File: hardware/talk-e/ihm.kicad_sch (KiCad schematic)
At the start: 17 parts, among them J1 Conn_01x04_Socket, SW1 SW_Push, SW2 SW_Push, SW3 SW_Push, SW4 SS-12D00-G 4 E, U1 RFM96W-433S2, U4 ESP32-S3

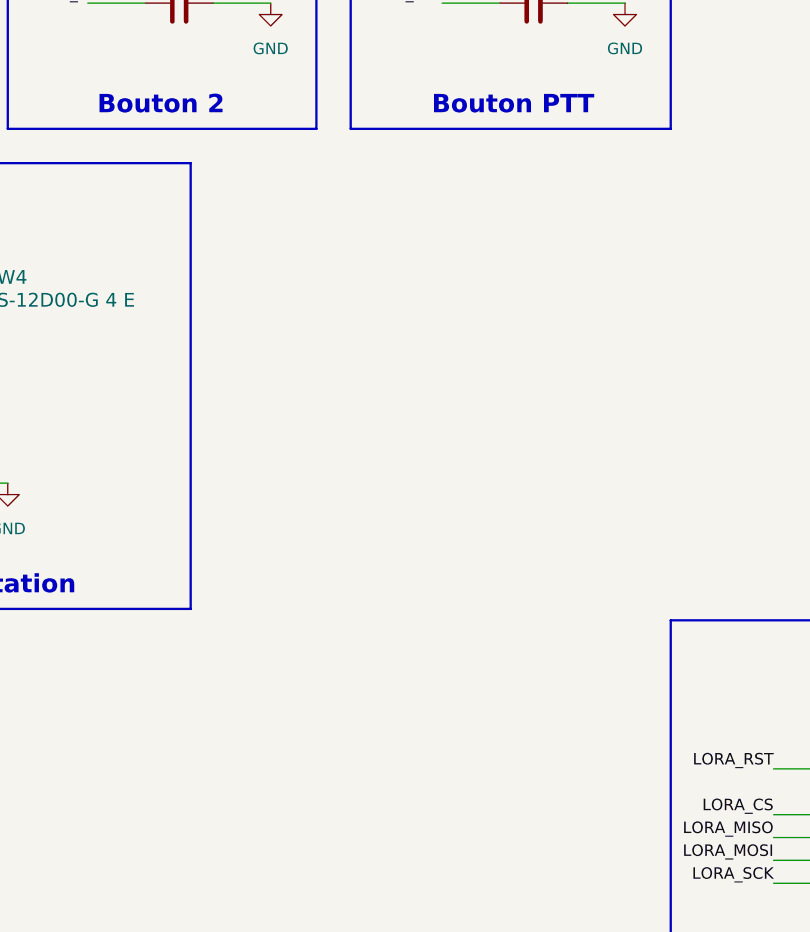
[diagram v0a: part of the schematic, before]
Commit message: Added vibration motor to schematic
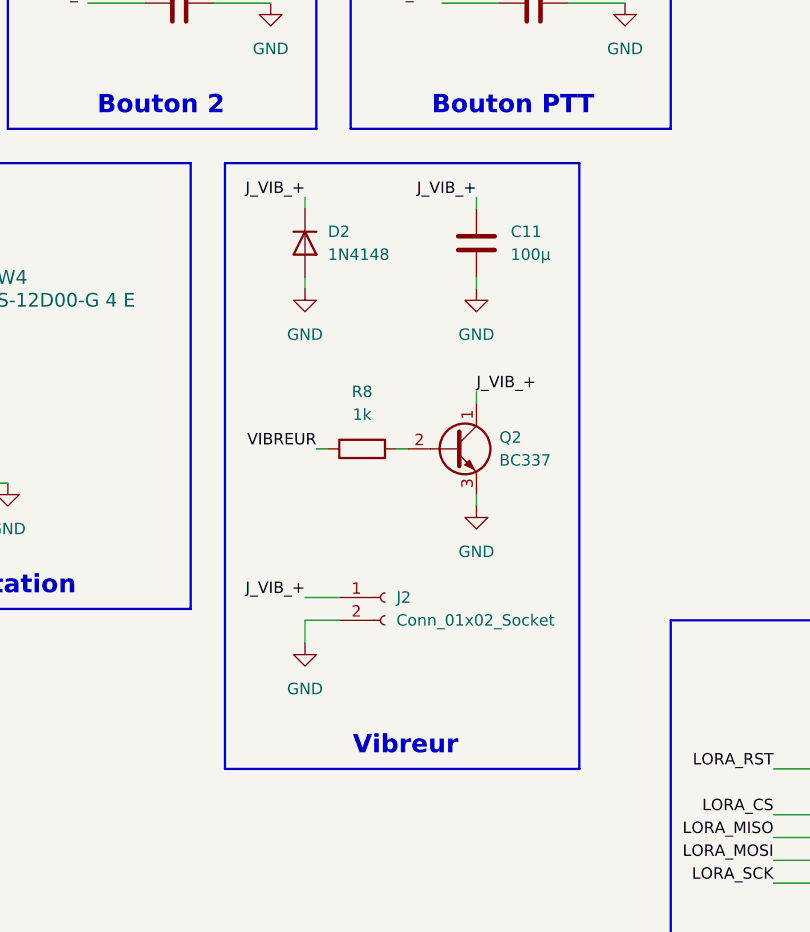
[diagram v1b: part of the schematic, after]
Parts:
- added C11: 100µ, symbol Device:C
- added D2: 1N4148, Diode_THT:D_DO-35_SOD27_P7.62mm_Horizontal, symbol Diode:1N4148
- added J2: Conn_01x02_Socket, Connector_JST:JST_EH_S2B-EH_1x02_P2.50mm_Horizontal, symbol Connector:Conn_01x02_Socket
- added Q2: BC337, Package_TO_SOT_THT:TO-92_Inline, symbol Transistor_BJT:BC337
- added R8: 1k, symbol Device:R
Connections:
- net GND: now also C11.2, D2.2 (A), J2.2 (Pin_2), Q2.3 (E)
- new net: Q2.2 (B), R8.2
- new net J_VIB_+: C11.1, D2.1 (K), J2.1 (Pin_1), Q2.1 (C)
- new net VIBREUR: R8.1
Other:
- note added: "Vibreur"

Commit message: Added RESET button and TX/RX LEDs to schematic
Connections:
- net BTN_1: no longer C10.1
- net SW_LOCK: now also C10.1
- net VIBREUR: now also U4.23 (GPIO17)
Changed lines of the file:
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@@
+	(wire
+		(pts
+			(xy 26.67 157.48) (xy 31.75 157.48)
+		)
+		(stroke
+			(width 0)
+			(type default)
+		)
+	)
 	(wire
 		(pts
@@
 		)
 	)
-	(label "BTN_1"
+	(label "SW_LOCK"
 		(at 118.11 92.71 180)
 		(effects
@@
 		(effects
 			(font
+				(size 1.27 1.27)
+			)
+			(justify right bottom)
+		)
+	)
+	(label "VIBREUR"
+		(at 26.67 157.48 180)
+		(effects
+			(font

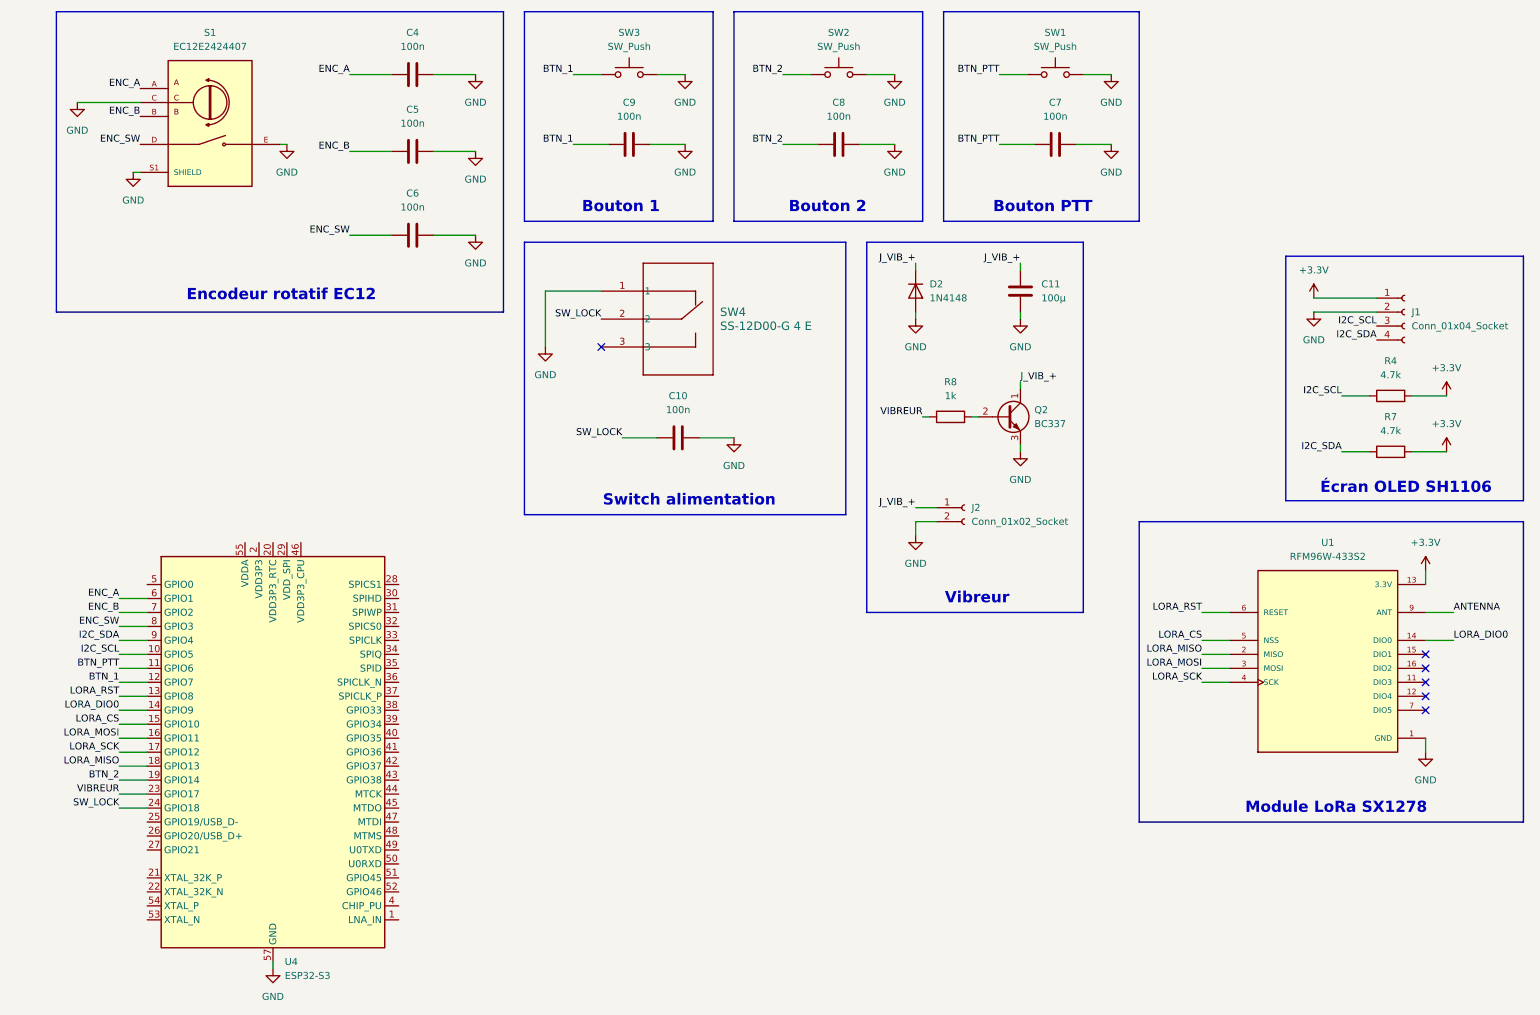
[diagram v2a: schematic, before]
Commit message: Added RESET button and TX/RX LEDs to schematic (2)
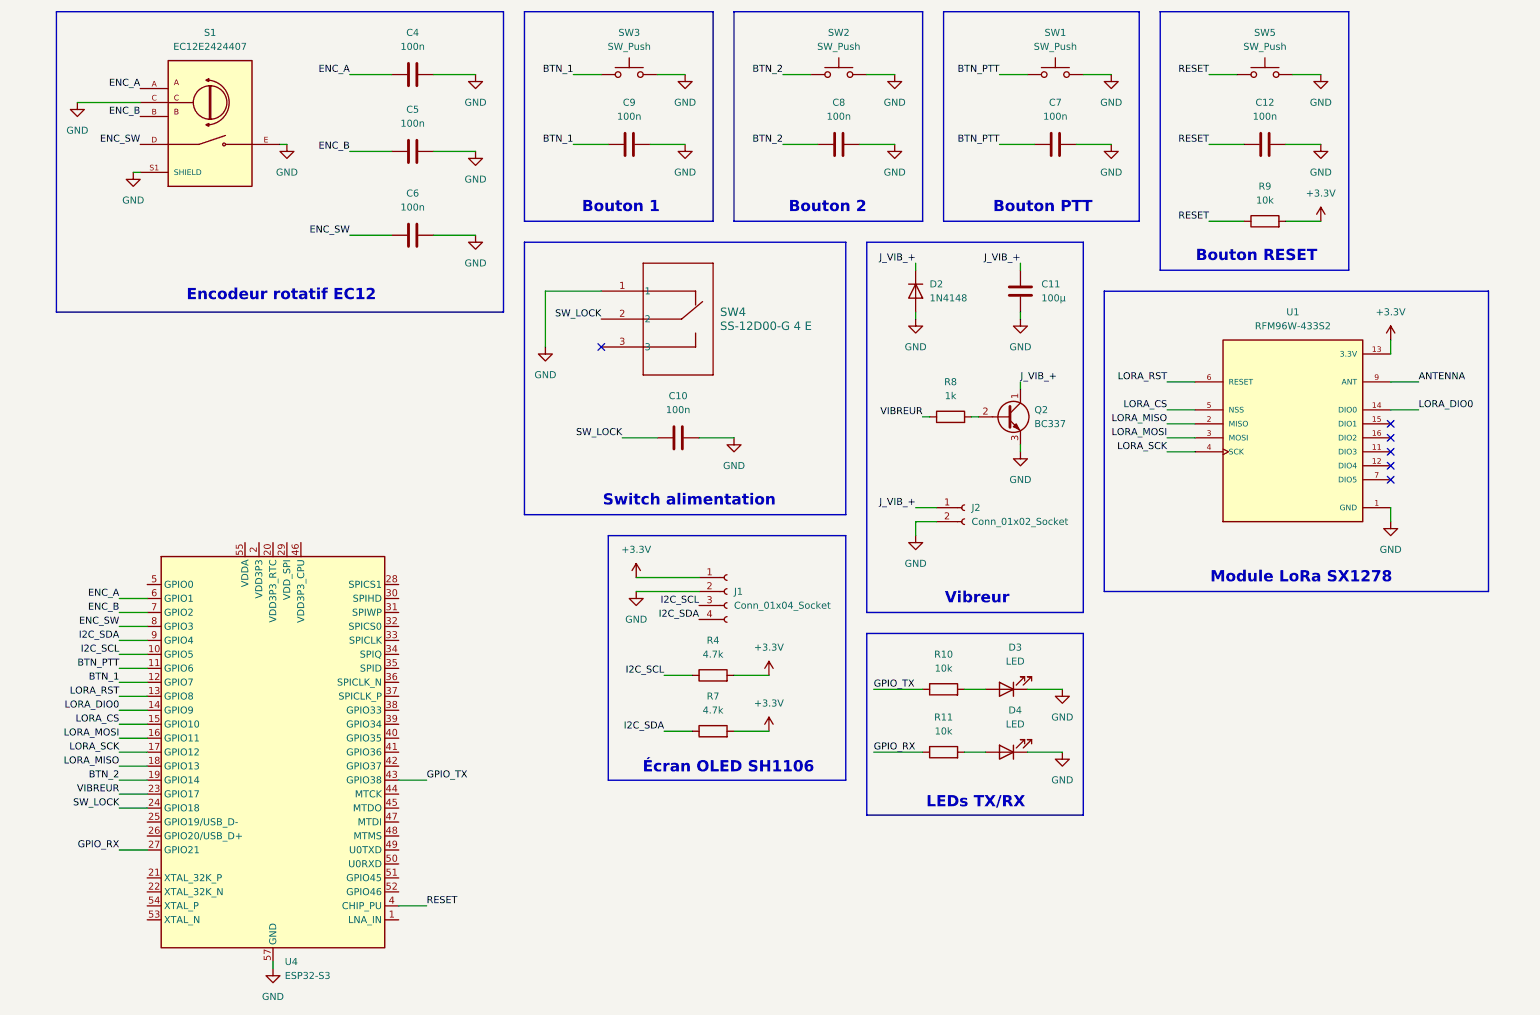
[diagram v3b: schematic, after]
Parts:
- added C12: 100n, symbol Device:C
- added D3, D4: LED, symbol Device:LED
- added R10, R11, R9: 10k, symbol Device:R
- added SW5: SW_Push, symbol Switch:SW_Push
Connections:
- net +3.3V: now also R9.2
- net GND: now also C12.2, D3.1 (K), D4.1 (K), SW5.2
- net GPIO_RX: now reaches U4.27 (GPIO21)
- net GPIO_RX: now also R11.1
- net RESET: now reaches U4.4 (CHIP_PU)
- net RESET: now also C12.1, R9.1, SW5.1
- net GPIO_TX: now reaches U4.43 (GPIO38)
- net GPIO_TX: now also R10.1
- new net: D3.2 (A), R10.2
- new net: D4.2 (A), R11.2
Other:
- note added: "Bouton RESET"
- note added: "LEDs TX/RX"
- moved on the sheet: J1, R4, R7, U1

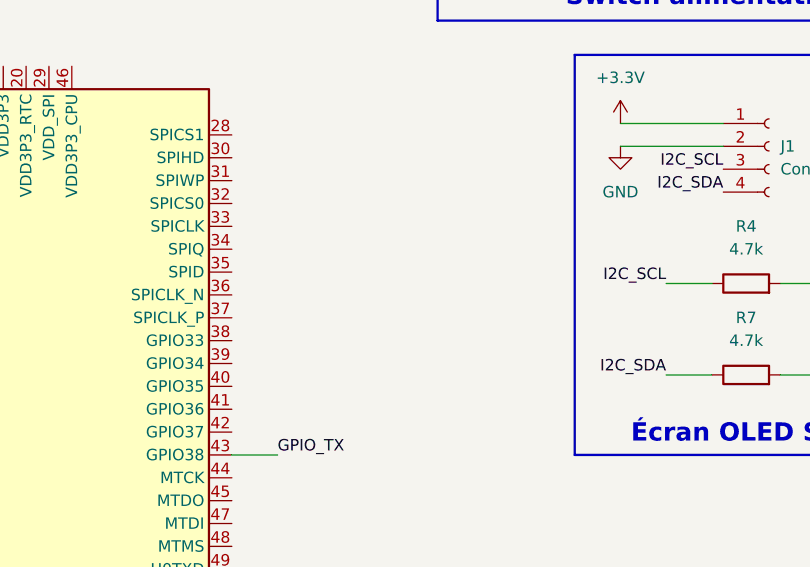
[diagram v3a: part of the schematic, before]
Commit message: Added TP4056, DW01A, AP2112K-3.3 to schematic
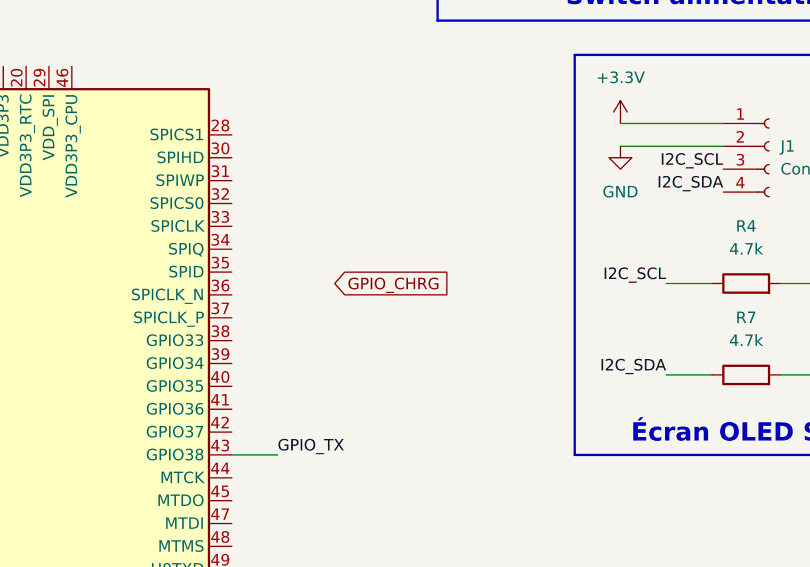
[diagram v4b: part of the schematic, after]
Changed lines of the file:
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@@
+		)
+	)
+	(global_label "GPIO_CHRG"
+		(shape input)
+		(at 88.9 135.89 0)
+		(fields_autoplaced yes)
+		(effects
+			(font
+				(size 1.27 1.27)
+			)
+			(justify left)
+		)
+		(property "Intersheetrefs" "${INTERSHEET_REFS}"
+			(at 102.4686 135.89 0)
+			(hide yes)
+			(show_name no)
+			(do_not_autoplace no)
+			(effects
+				(font
+					(size 1.27 1.27)
+				)
+				(justify left)
+			)
 		)
 	)

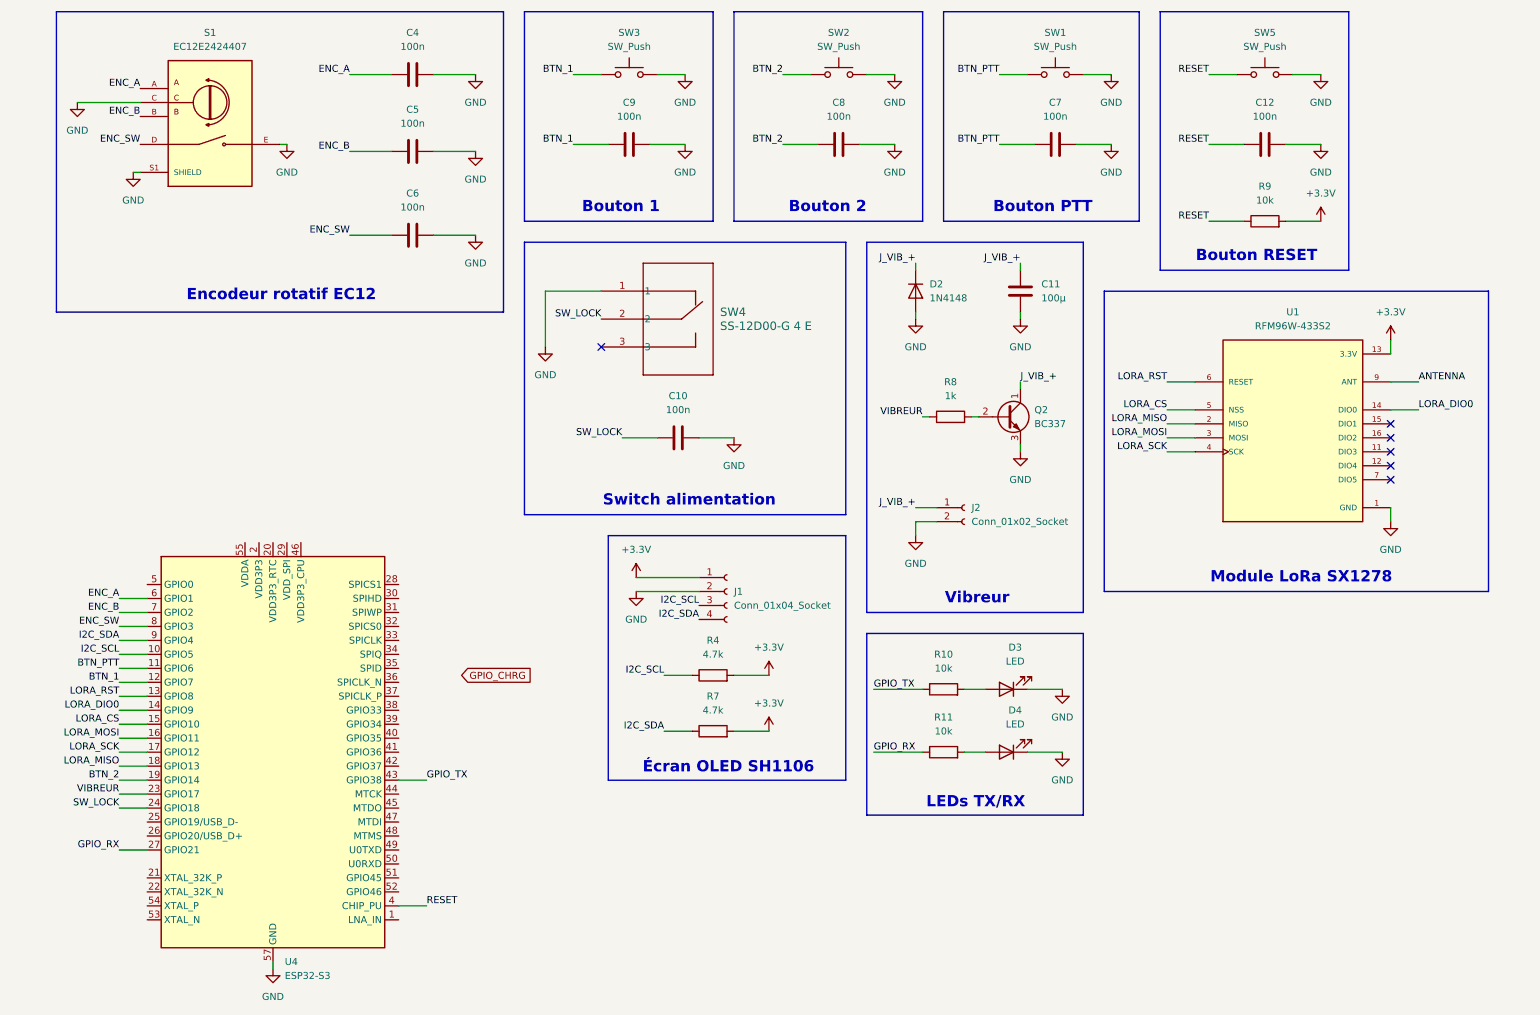
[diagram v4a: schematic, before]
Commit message: Added UART IDC connector, ESP32 decoupling capacitors
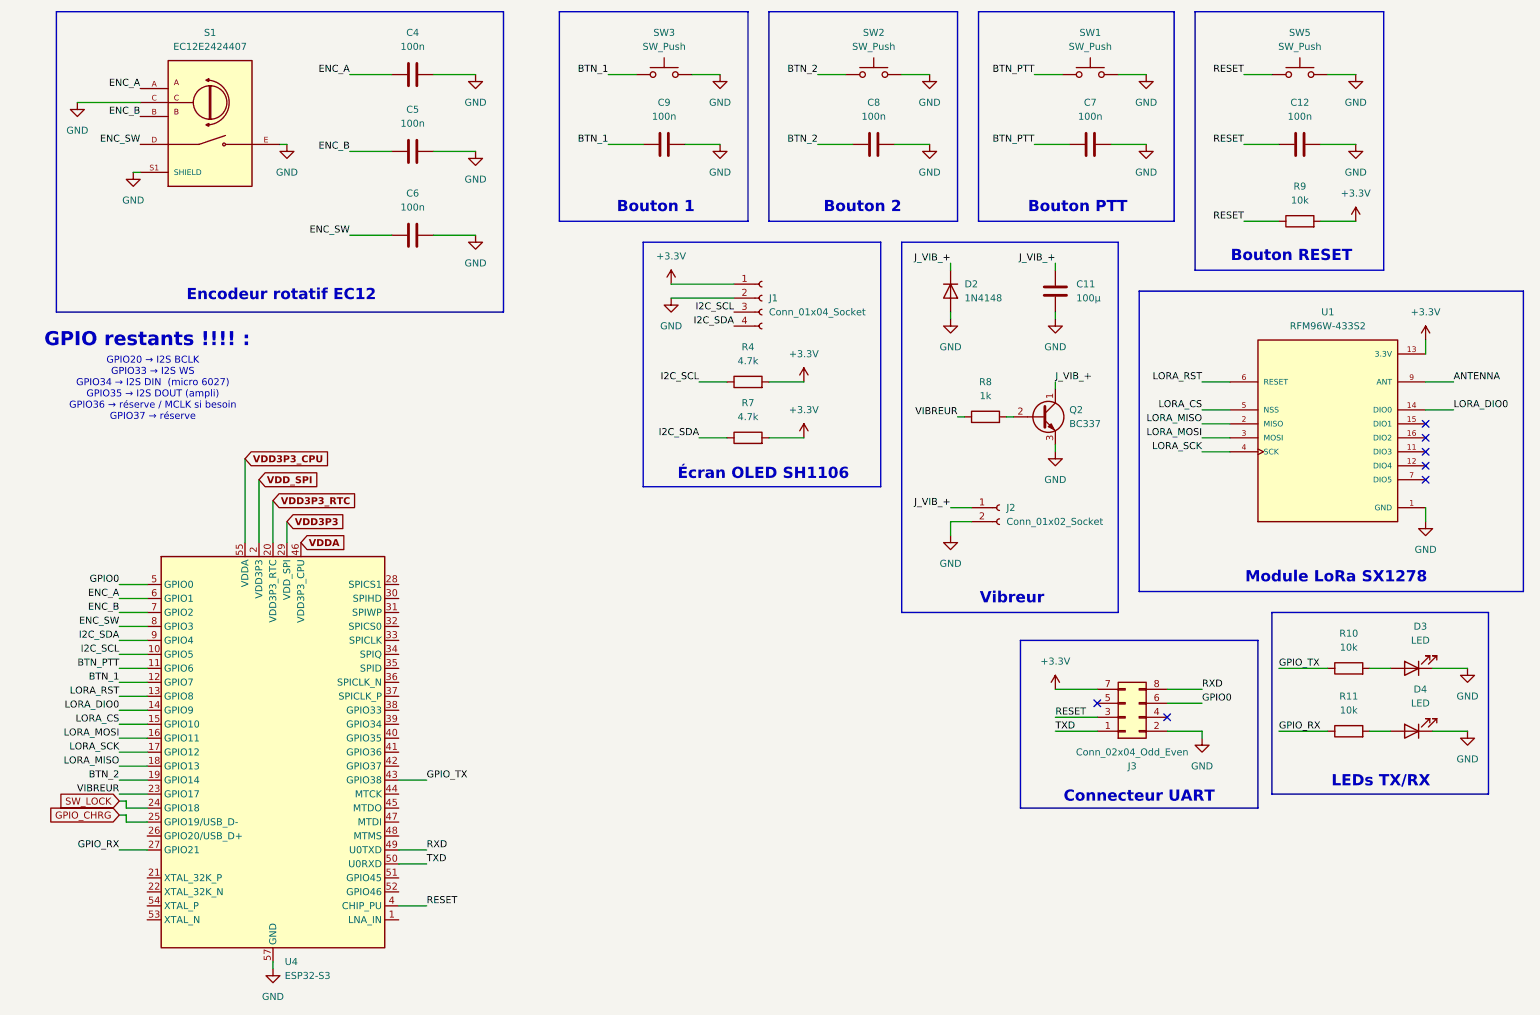
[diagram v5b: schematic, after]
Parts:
- removed C10: 100n, symbol Device:C
- removed SW4: SS-12D00-G 4 E, 1P2T_SS-12D00_CNK, symbol 2026-05-09_16-09-49:SS-12D00-G_4_E
- added J3: Conn_02x04_Odd_Even, Connector_IDC:IDC-Header_2x04_P2.54mm_Vertical, symbol Connector_Generic:Conn_02x04_Odd_Even
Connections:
- net +3.3V: now also J3.7 (Pin_7)
- net GND: now also J3.2 (Pin_2)
- net GPIO_CHRG: now also U4.25 (GPIO19/USB_D-)
- net RESET: now also J3.3 (Pin_3)
- net VDD_SPI: now reaches U4.2 (VDD3P3), U4.3 (VDD3P3)
- net VDD3P3_RTC: now reaches U4.20 (VDD3P3_RTC)
- net VDD3P3: now reaches U4.29 (VDD_SPI)
- net VDDA: now reaches U4.46 (VDD3P3_CPU)
- net RXD: now reaches U4.49 (U0TXD)
- net RXD: now also J3.8 (Pin_8)
- net GPIO0: now reaches U4.5 (GPIO0)
- net GPIO0: now also J3.6 (Pin_6)
- net TXD: now reaches U4.50 (U0RXD)
- net TXD: now also J3.1 (Pin_1)
- net VDD3P3_CPU: now reaches U4.55 (VDDA), U4.56 (VDDA)
- no-connect marks 6 -> 7
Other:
- note added: "Connecteur UART"
- note added: "GPIO restants !!!! :"
- note added: "GPIO20 → I2S BCLK GPIO33 → I2S WS GPIO34 → I2S DIN (micro 6027) GPIO35 → I2S DOUT (ampli) GPIO36 → réserve / MCLK si besoin GPIO37 → réserve"
- note removed: "Switch alimentation"
- moved on the sheet: C11, C12, C7, C8, C9, D2, D3, D4, J1, J2, Q2, R10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
